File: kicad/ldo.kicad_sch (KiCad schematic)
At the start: 5 parts, among them U3 MIC5365-3.3YD5

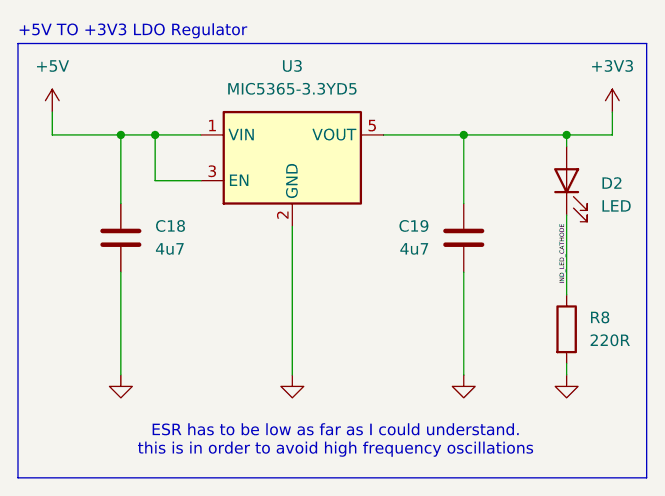
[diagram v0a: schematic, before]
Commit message: refactor(schematic): polish the schematic as much as possible - add new Basmala - fix netlist names almost EVERYWHERE, this is to help with net classes, and to help with building a good habit of naming nets properly - add a 100n capacitor to the SWD connector power pin - update many many other things EVERYWHERE
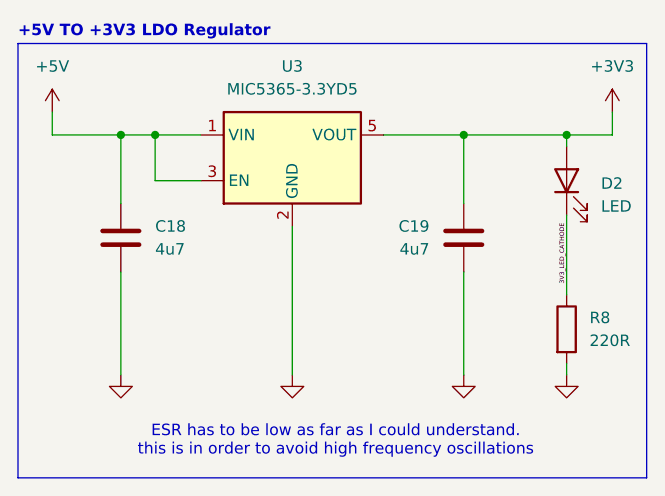
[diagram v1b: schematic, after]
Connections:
- net IND_LED_CATHODE renamed 3V3_LED_CATHODE
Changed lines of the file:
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@@
 			(font
 				(size 1.27 1.27)
+				(thickness 0.254)
+				(bold yes)
 			)
 			(justify left)
@@
 		)
 	)
-	(label "IND_LED_CATHODE"
+	(label "3V3_LED_CATHODE"
 		(at 172.72 106.68 90)
 		(effects
